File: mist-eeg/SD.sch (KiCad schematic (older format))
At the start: 11 parts, among them J5 Micro_SD_Card_Det, SW4 SD_RST

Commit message: Hooked-up the SoM
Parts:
- renumbered R101 to R100, R102 to R101, R103 to R102, R104 to R103, R97 to R96, R98 to R97, R99 to R98, R100 to R99, SW4 to SW3
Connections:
- net CON renamed ~CD~
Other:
- note added: "TODO:\n - add protection diodes\n - reset high-side switch"
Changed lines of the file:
@@
 $Descr USLetter 11000 8500
 encoding utf-8
-Sheet 12 12
+Sheet 11 12
 Title "Portiloop"
 Date "2021-06-07"
@@
 $EndComp
 $Comp
-L power:GND #PWR0120
+L power:GND #PWR0117
 U 1 1 60A29691
 P 4200 5200
-AR Path="/60A0E6BC/60A29691" Ref="#PWR0120"  Part="1"
+AR Path="/60A0E6BC/60A29691" Ref="#PWR0117"  Part="1"
 AR Path="/60A8612C/60A29691" Ref="#PWR?"  Part="1"
 AR Path="/60A7CCD6/60A29691" Ref="#PWR?"  Part="1"
-F 0 "#PWR0120" H 4200 4950 50  0001 C CNN
+F 0 "#PWR0117" H 4200 4950 50  0001 C CNN
 F 1 "GND" H 4205 5027 50  0000 C CNN
 F 2 "" H 4200 5200 50  0001 C CNN
@@
 	4250 4500 4200 4500
 $Comp
-L Device:R_Small R97
+L Device:R_Small R96
 U 1 1 60A2B32B
 P 3650 5150
-AR Path="/60A0E6BC/60A2B32B" Ref="R97"  Part="1"
+AR Path="/60A0E6BC/60A2B32B" Ref="R96"  Part="1"
 AR Path="/60A8612C/60A2B32B" Ref="R?"  Part="1"
 AR Path="/60A7CCD6/60A2B32B" Ref="R?"  Part="1"
-F 0 "R97" H 3591 5104 50  0000 R CNN
+F 0 "R96" H 3591 5104 50  0000 R CNN
 F 1 "4k7" H 3591 5195 50  0000 R CNN
 F 2 "Resistor_SMD:R_0201_0603Metric" H 3650 5150 50  0001 C CNN
@@
 	6000 5100 5950 5100
 Text HLabel 3500 5000 0    50   Output ~ 0
-CON
+~CD~
 Text Label 8800 4550 0    50   ~ 0
 +PWR
@@
 +PWR
 $Comp
-L Device:R_Small R98
+L Device:R_Small R97
 U 1 1 60A76D6B
 P 3850 4200
-AR Path="/60A0E6BC/60A76D6B" Ref="R98"  Part="1"
+AR Path="/60A0E6BC/60A76D6B" Ref="R97"  Part="1"
 AR Path="/60A8612C/60A76D6B" Ref="R?"  Part="1"
 AR Path="/60A7CCD6/60A76D6B" Ref="R?"  Part="1"
-F 0 "R98" V 3800 4300 50  0000 L CNN
+F 0 "R97" V 3800 4300 50  0000 L CNN
 F 1 "0R" V 3745 4200 50  0000 C CNN
 F 2 "Resistor_SMD:R_0603_1608Metric" H 3850 4200 50  0001 C CNN
@@
 $EndComp
 $Comp
-L Device:R_Small R99
+L Device:R_Small R98
 U 1 1 60A76E23
 P 3850 4300
-AR Path="/60A0E6BC/60A76E23" Ref="R99"  Part="1"
+AR Path="/60A0E6BC/60A76E23" Ref="R98"  Part="1"
 AR Path="/60A8612C/60A76E23" Ref="R?"  Part="1"
 AR Path="/60A7CCD6/60A76E23" Ref="R?"  Part="1"
-F 0 "R99" V 3800 4400 50  0000 L CNN
+F 0 "R98" V 3800 4400 50  0000 L CNN
 F 1 "0R" V 3745 4300 50  0001 C CNN
 F 2 "Resistor_SMD:R_0603_1608Metric" H 3850 4300 50  0001 C CNN
@@
 $EndComp
 $Comp
-L Device:R_Small R102
+L Device:R_Small R101
 U 1 1 60A76FE9
 P 3850 4800
-AR Path="/60A0E6BC/60A76FE9" Ref="R102"  Part="1"
+AR Path="/60A0E6BC/60A76FE9" Ref="R101"  Part="1"
 AR Path="/60A8612C/60A76FE9" Ref="R?"  Part="1"
 AR Path="/60A7CCD6/60A76FE9" Ref="R?"  Part="1"
-F 0 "R102" V 3800 4900 50  0000 L CNN
+F 0 "R101" V 3800 4900 50  0000 L CNN
 F 1 "0R" V 3745 4800 50  0001 C CNN
 F 2 "Resistor_SMD:R_0603_1608Metric" H 3850 4800 50  0001 C CNN
@@
 $EndComp
 $Comp
-L Device:R_Small R103
+L Device:R_Small R102
 U 1 1 60A7708B
 P 3850 4900
-AR Path="/60A0E6BC/60A7708B" Ref="R103"  Part="1"
+AR Path="/60A0E6BC/60A7708B" Ref="R102"  Part="1"
 AR Path="/60A8612C/60A7708B" Ref="R?"  Part="1"
 AR Path="/60A7CCD6/60A7708B" Ref="R?"  Part="1"
-F 0 "R103" V 3800 5000 50  0000 L CNN
+F 0 "R102" V 3800 5000 50  0000 L CNN
 F 1 "0R" V 3745 4900 50  0001 C CNN
 F 2 "Resistor_SMD:R_0603_1608Metric" H 3850 4900 50  0001 C CNN
@@
 $EndComp
 $Comp
-L Device:R_Small R104
+L Device:R_Small R103
 U 1 1 60A7712D
 P 3850 5000
-AR Path="/60A0E6BC/60A7712D" Ref="R104"  Part="1"
+AR Path="/60A0E6BC/60A7712D" Ref="R103"  Part="1"
 AR Path="/60A8612C/60A7712D" Ref="R?"  Part="1"
 AR Path="/60A7CCD6/60A7712D" Ref="R?"  Part="1"
-F 0 "R104" V 3800 5100 50  0000 L CNN
+F 0 "R103" V 3800 5100 50  0000 L CNN
 F 1 "0R" V 3745 5000 50  0001 C CNN
 F 2 "Resistor_SMD:R_0603_1608Metric" H 3850 5000 50  0001 C CNN
@@
 	8700 4400 8700 4550
 $Comp
-L Switch:SW_Push_Open SW4
+L Switch:SW_Push_Open SW3
 U 1 1 60E9F426
 P 8700 4200
-AR Path="/60A0E6BC/60E9F426" Ref="SW4"  Part="1"
+AR Path="/60A0E6BC/60E9F426" Ref="SW3"  Part="1"
 AR Path="/60A7CCD6/60E9F426" Ref="SW?"  Part="1"
-F 0 "SW4" V 8654 4278 50  0000 L CNN
+F 0 "SW3" V 8654 4278 50  0000 L CNN
 F 1 "SD_RST" V 8745 4278 50  0000 L CNN
 F 2 "Button_Switch_SMD:SW_SPST_TL3342" H 8700 4400 50  0001 C CNN
@@
 	3850 3900 3900 3900
 $Comp
-L power:GND #PWR0119
+L power:GND #PWR0116
 U 1 1 60ABC861
 P 3850 3900
-AR Path="/60A0E6BC/60ABC861" Ref="#PWR0119"  Part="1"
+AR Path="/60A0E6BC/60ABC861" Ref="#PWR0116"  Part="1"
 AR Path="/60A7CCD6/60ABC861" Ref="#PWR?"  Part="1"
-F 0 "#PWR0119" H 3850 3650 50  0001 C CNN
+F 0 "#PWR0116" H 3850 3650 50  0001 C CNN
 F 1 "GND" H 3855 3727 50  0000 C CNN
 F 2 "" H 3850 3900 50  0001 C CNN
@@
 	3650 5000 3750 5000
 $Comp
-L power:PWR_FLAG #FLG06
+L power:PWR_FLAG #FLG05
 U 1 1 610BF823
 P 8650 4550
-AR Path="/60A0E6BC/610BF823" Ref="#FLG06"  Part="1"
+AR Path="/60A0E6BC/610BF823" Ref="#FLG05"  Part="1"
 AR Path="/60A7CCD6/610BF823" Ref="#FLG?"  Part="1"
-F 0 "#FLG06" H 8650 4625 50  0001 C CNN
+F 0 "#FLG05" H 8650 4625 50  0001 C CNN
 F 1 "PWR_FLAG" V 8650 4677 50  0000 L CNN
 F 2 "" H 8650 4550 50  0001 C CNN
@@
 	3950 4800 4250 4800
 $Comp
-L Device:R_Small R100
+L Device:R_Small R99
 U 1 1 60A76EC5
 P 3850 4400
-AR Path="/60A0E6BC/60A76EC5" Ref="R100"  Part="1"
+AR Path="/60A0E6BC/60A76EC5" Ref="R99"  Part="1"
 AR Path="/60A8612C/60A76EC5" Ref="R?"  Part="1"
 AR Path="/60A7CCD6/60A76EC5" Ref="R?"  Part="1"
-F 0 "R100" V 3800 4500 50  0000 L CNN
+F 0 "R99" V 3800 4500 50  0000 L CNN
 F 1 "0R" V 3745 4400 50  0001 C CNN
 F 2 "Resistor_SMD:R_0603_1608Metric" H 3850 4400 50  0001 C CNN
@@
 $EndComp
 $Comp
-L Device:R_Small R101
+L Device:R_Small R100
 U 1 1 60A76F57
 P 3850 4600
-AR Path="/60A0E6BC/60A76F57" Ref="R101"  Part="1"
+AR Path="/60A0E6BC/60A76F57" Ref="R100"  Part="1"
 AR Path="/60A8612C/60A76F57" Ref="R?"  Part="1"
 AR Path="/60A7CCD6/60A76F57" Ref="R?"  Part="1"
-F 0 "R101" V 3800 4700 50  0000 L CNN
+F 0 "R100" V 3800 4700 50  0000 L CNN
 F 1 "0R" V 3745 4600 50  0001 C CNN
 F 2 "Resistor_SMD:R_0603_1608Metric" H 3850 4600 50  0001 C CNN
@@
 	3650 4900 3750 4900
 $Comp
-L power:+3V3 #PWR0118
+L power:+3V3 #PWR0115
 U 1 1 6116A372
 P 3600 5300
-F 0 "#PWR0118" H 3600 5150 50  0001 C CNN
+F 0 "#PWR0115" H 3600 5150 50  0001 C CNN
 F 1 "+3V3" V 3615 5428 50  0000 L CNN
 F 2 "" H 3600 5300 50  0001 C CNN
@@
 Text HLabel 8700 3950 1    50   Input ~ 0
 +PWR_IN
+Text Notes 4350 5900 0    50   ~ 0
+TODO:\n - add protection diodes\n - reset high-side switch
+Text HLabel 8450 4200 0    50   Input ~ 0
+~RST~
 $EndSCHEMATC

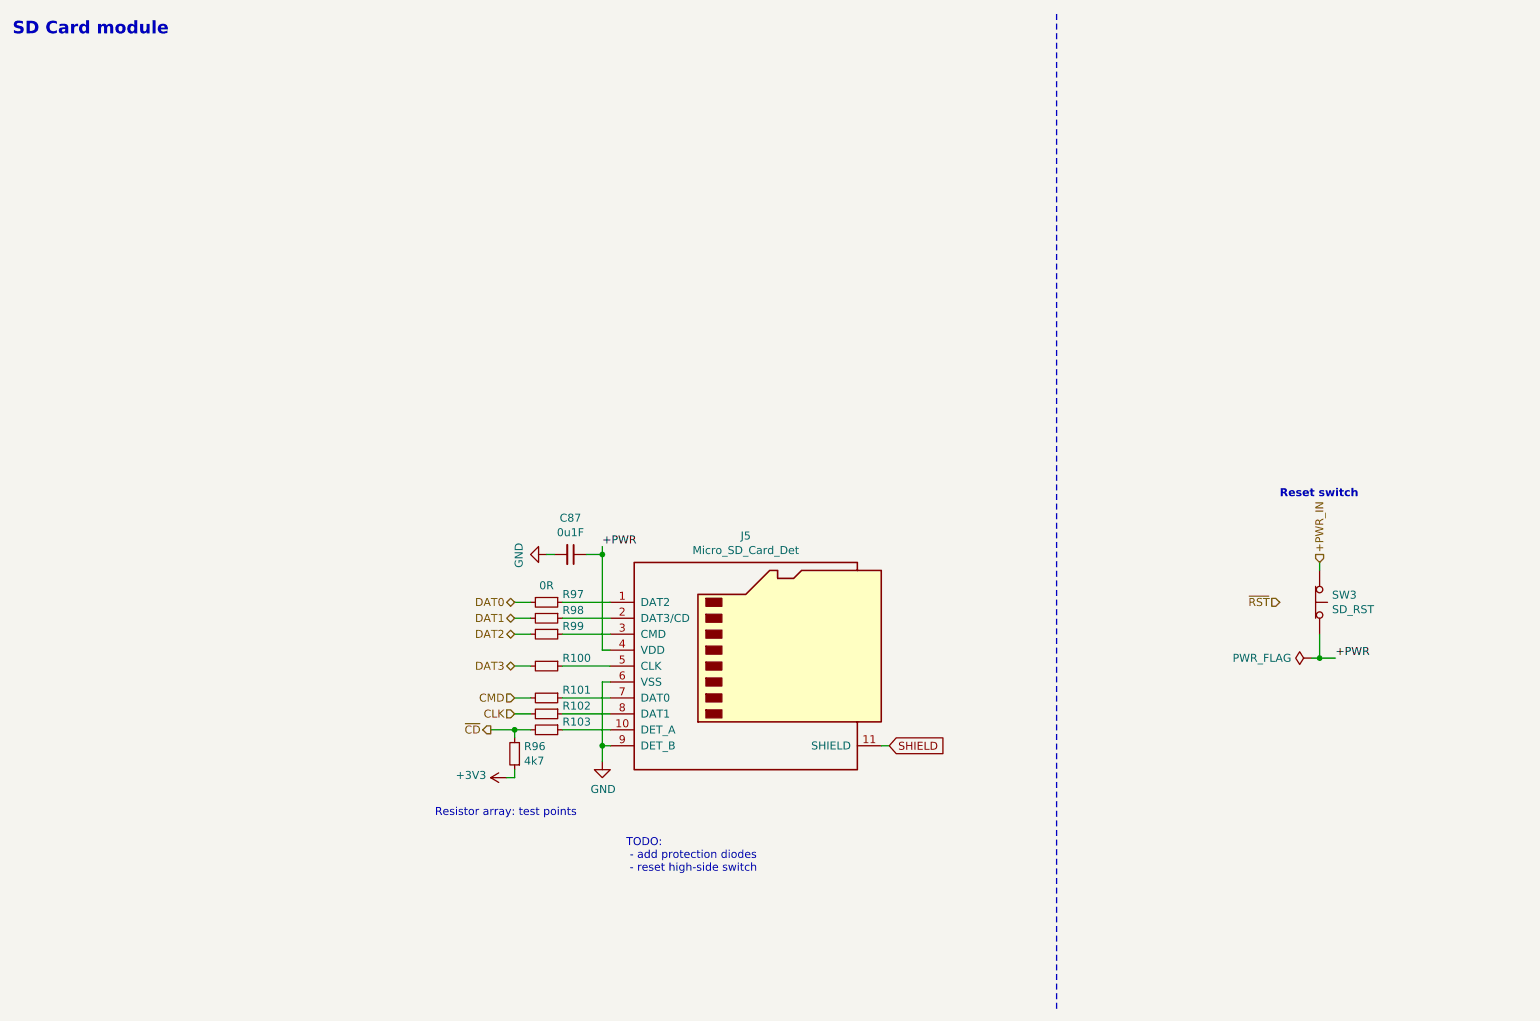
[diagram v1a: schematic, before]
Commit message: Finish schematic and create interface specifications
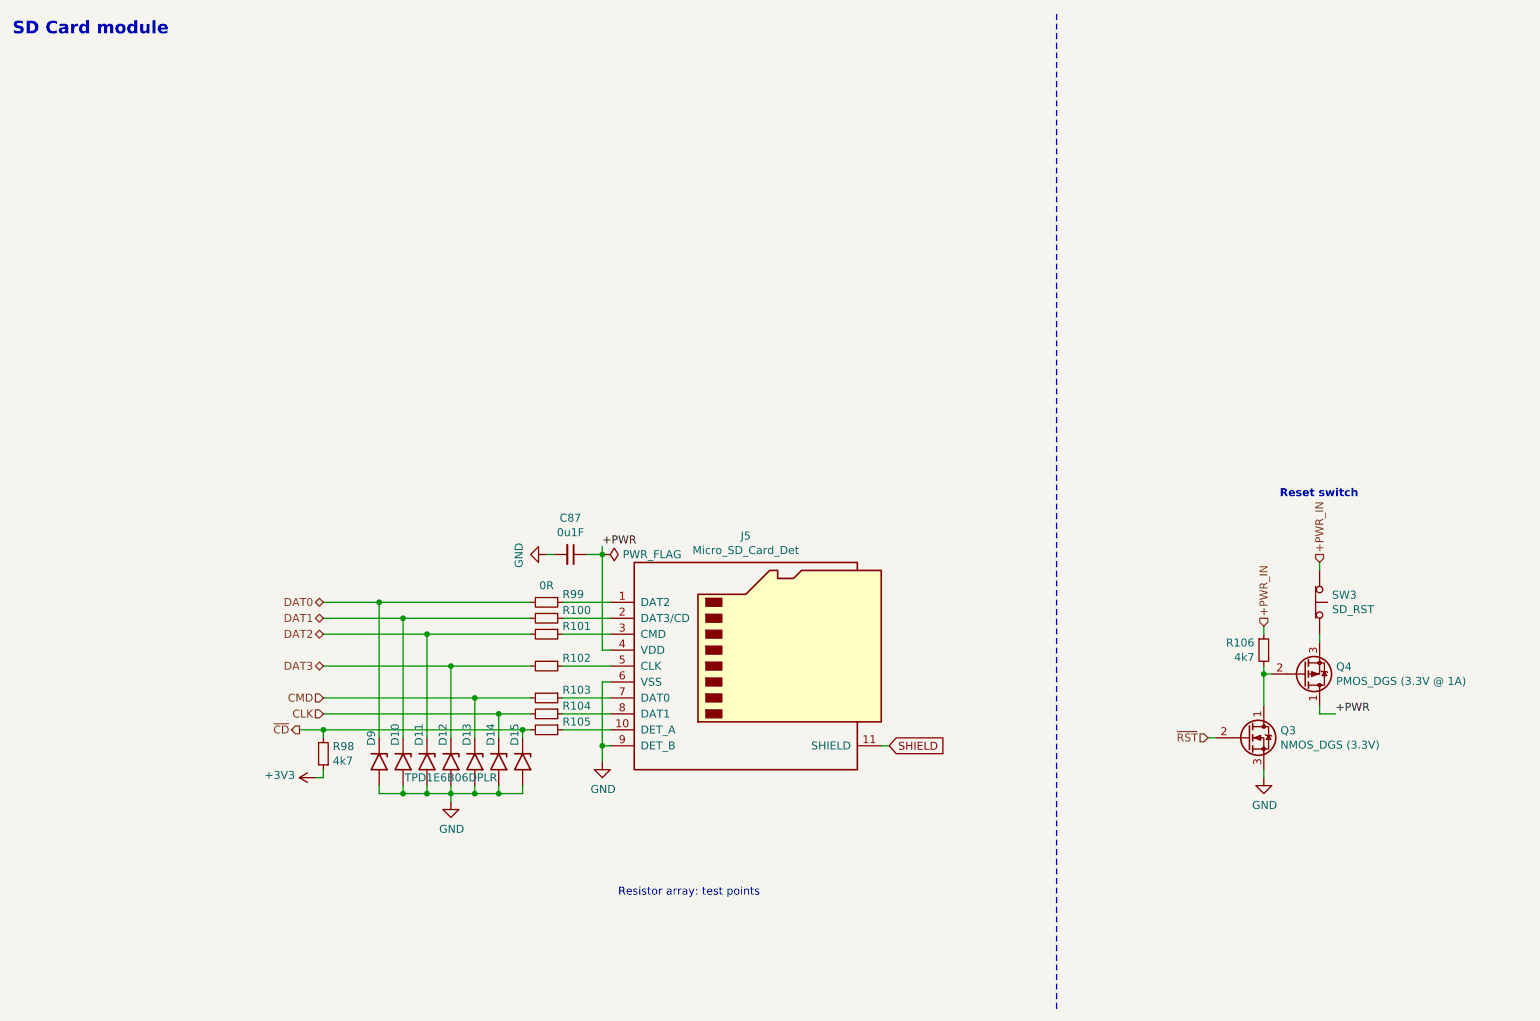
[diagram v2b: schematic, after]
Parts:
- added D10, D11, D12, D13, D14, D15, D9: TPD1E6B06DPLR, Diode_SMD:D_0201_0603Metric, symbol Diode:SM6T6V8A
- added Q3: NMOS_DGS (3.3V), Package_TO_SOT_SMD:SOT-23, symbol Device:Q_NMOS_DGS
- added Q4: PMOS_DGS (3.3V @ 1A), Package_TO_SOT_SMD:SOT-23, symbol Device:Q_PMOS_DGS
- added R106: 4k7, Resistor_SMD:R_0201_0603Metric, symbol Device:R_Small
- renumbered R98 to R100, R99 to R101, R100 to R102, R101 to R103, R102 to R104, R103 to R105, R96 to R98, R97 to R99
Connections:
- net +PWR: now also Q4.1 (D); no longer SW3.2 (B)
- net +PWR_IN: now also R106.1
- net CLK: now also D14.1 (A1)
- net CMD: now also D13.1 (A1)
- net DAT0: now also D9.1 (A1)
- net DAT1: now also D10.1 (A1)
- net DAT2: now also D11.1 (A1)
- net DAT3: now also D12.1 (A1)
- net GND: now also D10.2 (A2), D11.2 (A2), D12.2 (A2), D13.2 (A2), D14.2 (A2), D15.2 (A2), D9.2 (A2), Q3.3 (S)
- net ~CD~: now also D15.1 (A1)
- net ~RST~: now also Q3.2 (G)
- new net: Q4.3 (S), SW3.2 (B)
- new net: Q3.1 (D), Q4.2 (G), R106.2
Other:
- note removed: "TODO:\n - add protection diodes\n - reset high-side switch"
- moved on the sheet: R98

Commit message: Advance routing
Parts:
- added FB1: Ferrite_Bead_Small, Resistor_SMD:R_0603_1608Metric, symbol Device:Ferrite_Bead_Small
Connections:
- net GND: now also FB1.1
- net SHIELD: no longer names the net of J5.11 (SHIELD)
- net SHIELD: now also FB1.2
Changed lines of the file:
@@
 $Descr USLetter 11000 8500
 encoding utf-8
-Sheet 11 12
+Sheet 10 11
 Title "Portiloop"
 Date "2021-06-07"
@@
 Wire Wire Line
 	4200 5100 4200 5200
-Text GLabel 6000 5100 2    50   Input ~ 0
-SHIELD
 Wire Wire Line
 	6000 5100 5950 5100
@@
 F 3 "~" H 8700 4400 50  0001 C CNN
 	1    8700 4200
-	0    1    1    0
-$EndComp
-Wire Wire Line
-	3850 3900 3900 3900
-$Comp
-L power:GND #PWR0118
-U 1 1 60ABC861
-P 3850 3900
-AR Path="/60A0E6BC/60ABC861" Ref="#PWR0118"  Part="1"
-AR Path="/60A7CCD6/60ABC861" Ref="#PWR?"  Part="1"
-F 0 "#PWR0118" H 3850 3650 50  0001 C CNN
-F 1 "GND" H 3855 3727 50  0000 C CNN
-F 2 "" H 3850 3900 50  0001 C CNN
-F 3 "" H 3850 3900 50  0001 C CNN
-	1    3850 3900
 	0    1    1    0
 $EndComp
@@
 	1    0    0    1
 $EndComp
+$Comp
+L power:GND #PWR0118
+U 1 1 6130D5F8
+P 3850 3900
+F 0 "#PWR0118" H 3850 3650 50  0001 C CNN
+F 1 "GND" V 3855 3772 50  0000 R CNN
+F 2 "" H 3850 3900 50  0001 C CNN
+F 3 "" H 3850 3900 50  0001 C CNN
+	1    3850 3900
+	0    1    1    0
+$EndComp
+Wire Wire Line
+	3850 3900 3900 3900
+Wire Wire Line
+	6200 5100 6250 5100
+$Comp
+L power:GND #PWR?
+U 1 1 610A6E66
+P 6250 5100
+AR Path="/610A6E66" Ref="#PWR?"  Part="1"
+AR Path="/60A0E6BC/610A6E66" Ref="#PWR0138"  Part="1"
+F 0 "#PWR0138" H 6250 4850 50  0001 C CNN
+F 1 "GND" V 6255 4972 50  0000 R CNN
+F 2 "" H 6250 5100 50  0001 C CNN
+F 3 "" H 6250 5100 50  0001 C CNN
+	1    6250 5100
+	0    -1   -1   0
+$EndComp
+$Comp
+L Device:Ferrite_Bead_Small FB?
+U 1 1 610A6E6C
+P 6100 5100
+AR Path="/609A79EB/60EAD252/610A6E6C" Ref="FB?"  Part="1"
+AR Path="/609A79EB/60BBE340/610A6E6C" Ref="FB?"  Part="1"
+AR Path="/610A6E6C" Ref="FB?"  Part="1"
+AR Path="/60A0E6BC/610A6E6C" Ref="FB1"  Part="1"
+F 0 "FB1" V 6245 5100 50  0000 C CNN
+F 1 "Ferrite_Bead_Small" V 6336 5100 50  0000 C CNN
+F 2 "Resistor_SMD:R_0603_1608Metric" V 6030 5100 50  0001 C CNN
+F 3 "~" H 6100 5100 50  0001 C CNN
+	1    6100 5100
+	0    1    1    0
+$EndComp
 $EndSCHEMATC

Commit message: Validation & fabrication layer
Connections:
- net +PWR: now also SW3.2 (B); no longer Q4.1 (D)
- net +PWR_IN: now also Q4.3 (S); no longer SW3.1 (A)
- new net: Q4.1 (D), SW3.1 (A)
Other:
- moved on the sheet: SW3
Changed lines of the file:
@@
 Text HLabel 2300 5000 0    50   Output ~ 0
 ~CD~
-Text Label 8800 4900 0    50   ~ 0
+Text Label 9250 5400 0    50   ~ 0
 +PWR
 Text Label 4200 3850 0    50   ~ 0
@@
 	7050 6750 7050 500
 Wire Wire Line
-	8700 3950 8700 4000
+	8700 4400 8700 4450
 $Comp
 L Switch:SW_Push_Open SW3
 U 1 1 60E9F426
-P 8700 4200
+P 9200 5150
 AR Path="/60A0E6BC/60E9F426" Ref="SW3"  Part="1"
 AR Path="/60A7CCD6/60E9F426" Ref="SW?"  Part="1"
-F 0 "SW3" V 8654 4278 50  0000 L CNN
-F 1 "SD_RST" V 8745 4278 50  0000 L CNN
-F 2 "Button_Switch_SMD:SW_SPST_TL3342" H 8700 4400 50  0001 C CNN
-F 3 "~" H 8700 4400 50  0001 C CNN
-	1    8700 4200
+F 0 "SW3" V 9154 5228 50  0000 L CNN
+F 1 "SD_RST" V 9245 5228 50  0000 L CNN
+F 2 "Button_Switch_SMD:SW_SPST_TL3342" H 9200 5350 50  0001 C CNN
+F 3 "~" H 9200 5350 50  0001 C CNN
+	1    9200 5150
 	0    1    1    0
 $EndComp
@@
 Wire Wire Line
 	2400 5300 2450 5300
-Text HLabel 8700 3950 1    50   Input ~ 0
+Text HLabel 8700 4400 1    50   Input ~ 0
 +PWR_IN
 Text HLabel 8000 5050 0    50   Input ~ 0
@@
 Wire Wire Line
 	8700 4850 8700 4900
-Wire Wire Line
-	8700 4450 8700 4400
 $Comp
 L Device:Q_NMOS_DGS Q3
@@
 Wire Wire Line
 	8350 4650 8400 4650
-Wire Wire Line
-	8800 4900 8700 4900
 Wire Wire Line
 	8350 4650 8350 4850
@@
 	0    1    1    0
 $EndComp
+Wire Wire Line
+	9250 5400 9200 5400
+Wire Wire Line
+	9200 5400 9200 5350
+Wire Wire Line
+	9200 4900 9200 4950
+Wire Wire Line
+	8700 4900 9200 4900
 $EndSCHEMATC

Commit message: Update footprints based upon piece availability & generate manufacturing files
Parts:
- added Q2: NMOS_DGS (3.3V), Package_TO_SOT_SMD:SOT-23, symbol Device:Q_NMOS_DGS
- added R11: 4k7, Resistor_SMD:R_0201_0603Metric, symbol Device:R_Small
- J5: footprint Connector_Card:microSD_HC_Hirose_DM3AT-SF-PEJM5 -> Connector_Card:microSD_HC_Molex_104031-0811
- SW3: symbol Switch:SW_Push_Open -> Switch:SW_Push
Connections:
- net +PWR: now also Q4.1 (D); no longer SW3.2 (B)
- net +PWR_IN: now also R11.1
- net GND: now also SW3.1
- net at Q4.2 (G), R106.2: now also Q2.1 (D); no longer Q3.1 (D)
- new net: Q2.2 (G), R11.2, SW3.2
- new net: Q2.3 (S), Q3.1 (D)
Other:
- moved on the sheet: C87, D10, D11, D12, D13, D14, D15, D9, FB1, J5, Q3, Q4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

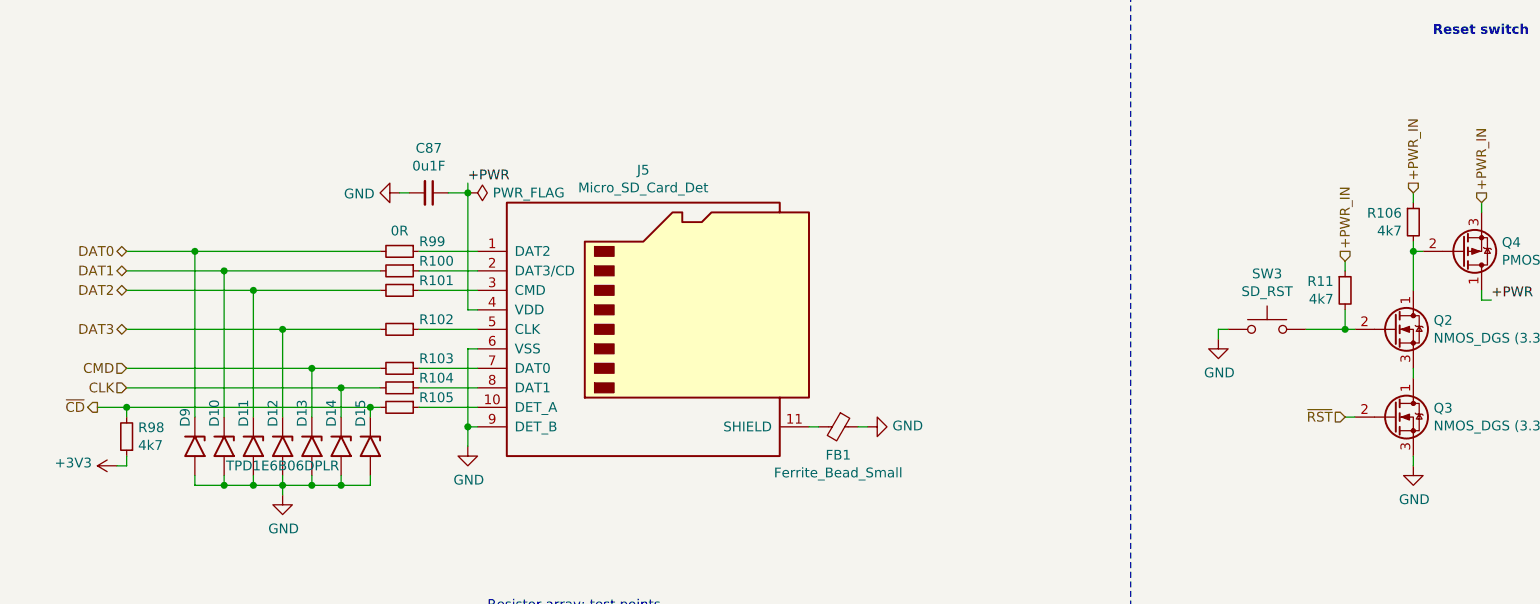
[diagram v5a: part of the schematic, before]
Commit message: Change buckboost regulator used
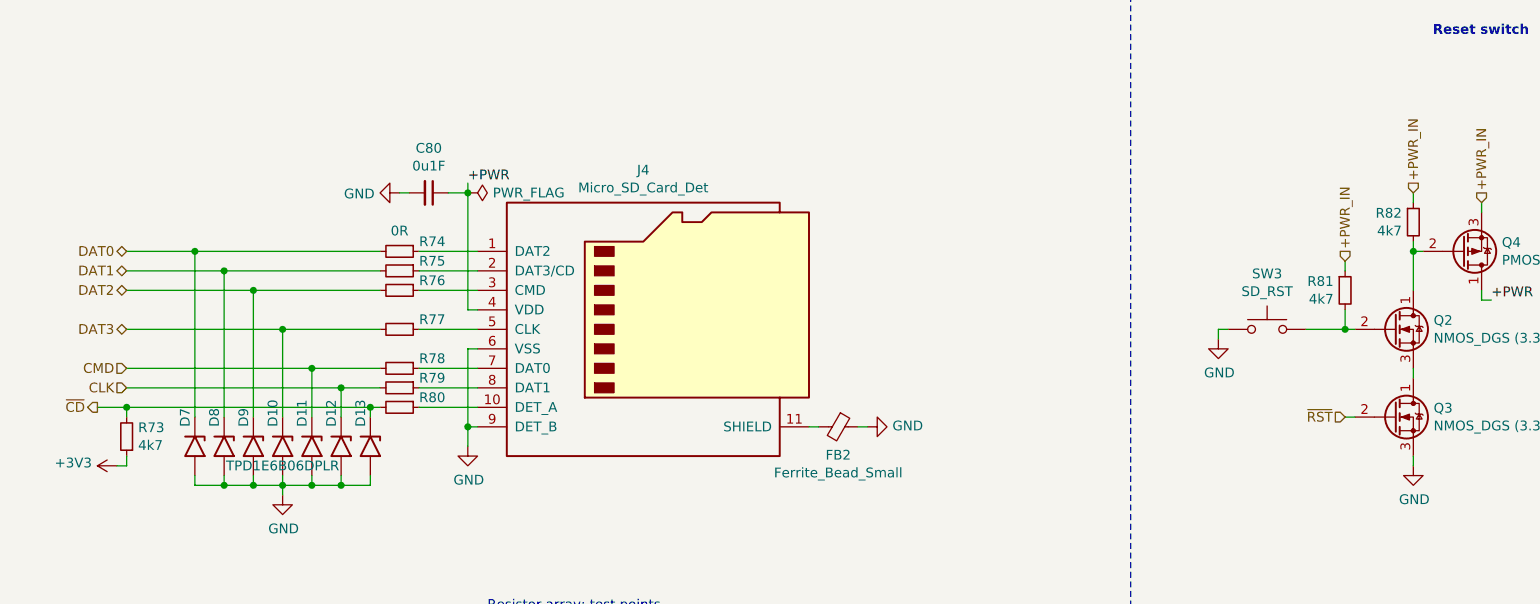
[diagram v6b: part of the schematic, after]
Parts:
- renumbered C87 to C80, D12 to D10, D13 to D11, D14 to D12, D15 to D13, D9 to D7, D10 to D8, D11 to D9, FB1 to FB2, J5 to J4, R98 to R73, R99 to R74, R100 to R75, R101 to R76, R102 to R77, R103 to R78, R104 to R79, R105 to R80, R11 to R81, R106 to R82
